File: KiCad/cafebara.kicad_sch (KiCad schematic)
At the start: 26 parts, among them J1 Micro_SD_Card_Det2, J2 USB_C_Receptacle_USB2.0_14P, J3 PROG, J4 505278-1933, J5 I2C, Q1 NMOS, SW1 SW_Push, U3 ATtiny1616-M

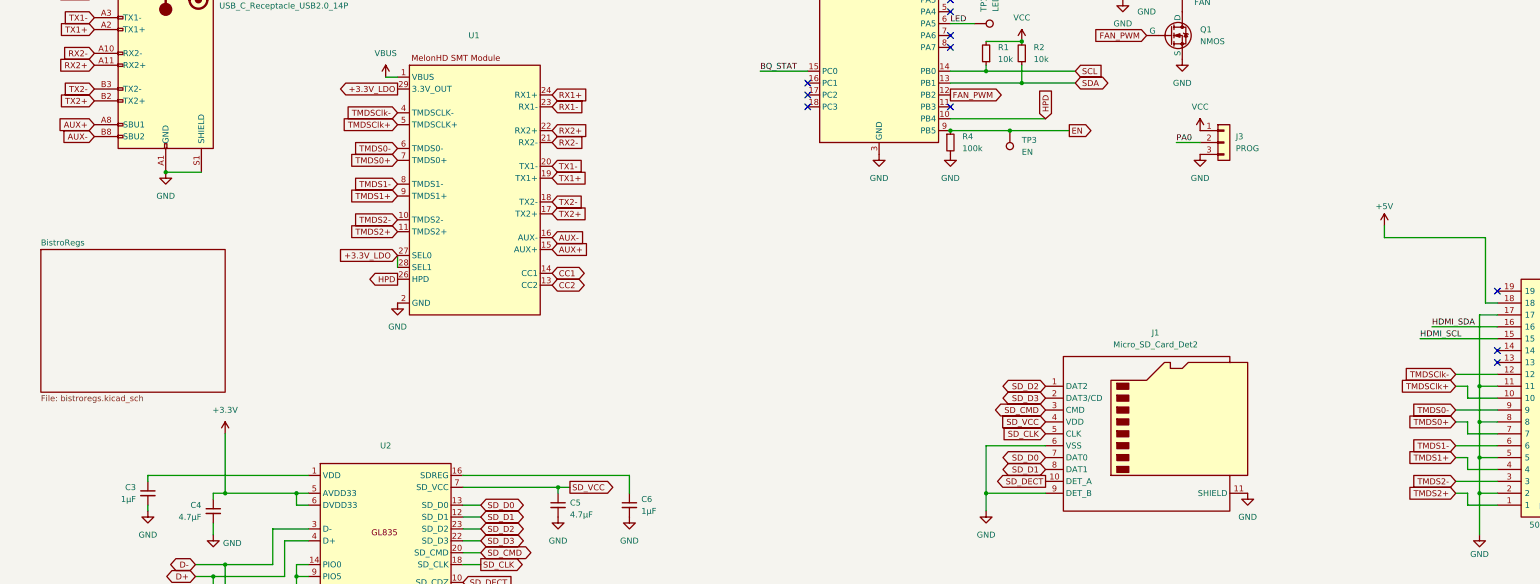
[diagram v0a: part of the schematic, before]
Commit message: Split regs into separate KiCad project
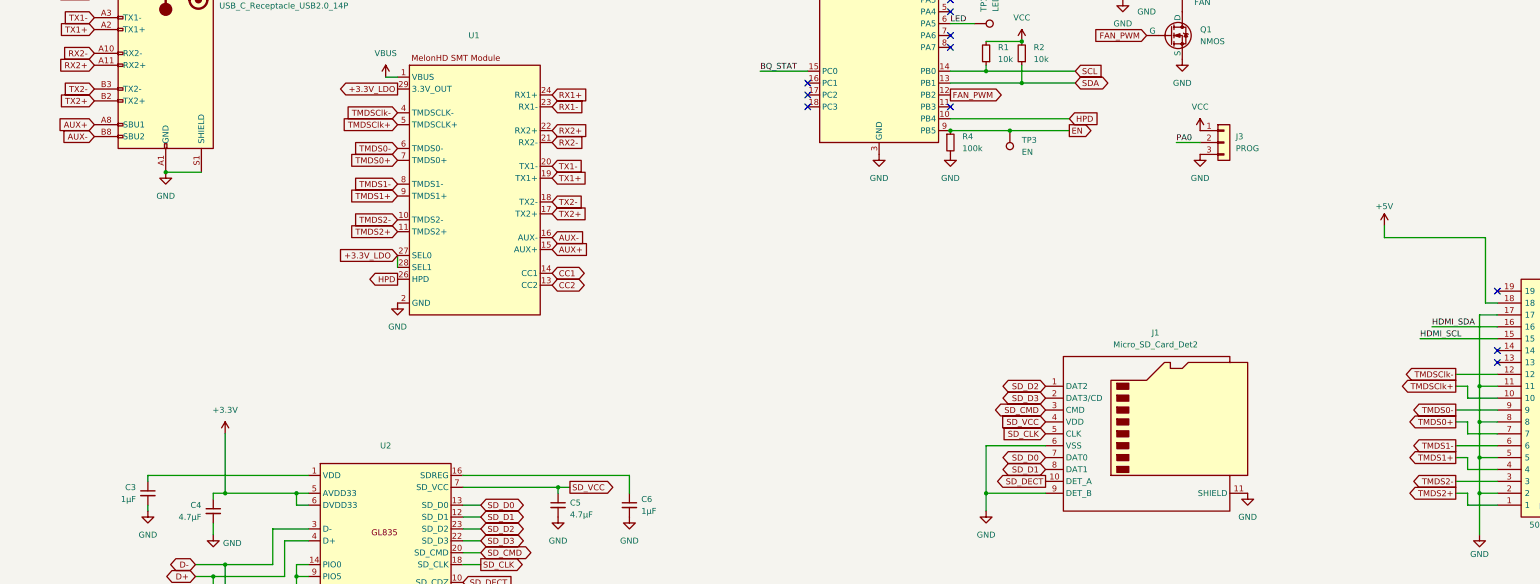
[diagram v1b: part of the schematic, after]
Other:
- removed sheet BistroRegs
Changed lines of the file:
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@@
 	(wire
 		(pts
-			(xy 217.17 76.2) (xy 237.49 76.2)
+			(xy 217.17 76.2) (xy 242.57 76.2)
 		)
 		(stroke
@@
 	)
 	(global_label "TMDS1-"
-		(shape input)
+		(shape output)
 		(at 325.12 146.05 180)
 		(fields_autoplaced yes)
@@
 	)
 	(global_label "TMDS0-"
-		(shape input)
+		(shape output)
 		(at 325.12 138.43 180)
 		(fields_autoplaced yes)
@@
 	)
 	(global_label "TMDS1+"
-		(shape input)
+		(shape output)
 		(at 325.12 148.59 180)
 		(fields_autoplaced yes)
@@
 	(global_label "HPD"
 		(shape input)
-		(at 237.49 76.2 90)
+		(at 242.57 76.2 0)
 		(fields_autoplaced yes)
 		(effects
@@
 		)
 		(property "Intersheetrefs" "${INTERSHEET_REFS}"
-			(at 237.49 69.3443 90)
+			(at 249.4257 76.2 0)
 			(effects
 				(font
@@
 	)
 	(global_label "TMDS2-"
-		(shape input)
+		(shape output)
 		(at 325.12 153.67 180)
 		(fields_autoplaced yes)
@@
 	)
 	(global_label "TMDSClk+"
-		(shape input)
+		(shape output)
 		(at 325.12 133.35 180)
 		(fields_autoplaced yes)
@@
 	)
 	(global_label "TMDSClk-"
-		(shape input)
+		(shape output)
 		(at 325.12 130.81 180)
 		(fields_autoplaced yes)
@@
 	)
 	(global_label "TMDS0+"
-		(shape input)
+		(shape output)
 		(at 325.12 140.97 180)
 		(fields_autoplaced yes)
@@
 	)
 	(global_label "TMDS2+"
-		(shape input)
+		(shape output)
 		(at 325.12 156.21 180)
 		(fields_autoplaced yes)
@@
 				)
 			)
-		)
-	)
-	(sheet
-		(at 22.86 104.14)
-		(size 39.37 30.48)
-		(exclude_from_sim no)
-		(in_bom yes)
-		(on_board yes)
-		(dnp no)
-		(fields_autoplaced yes)
-		(stroke
-			(width 0.1524)
-			(type solid)
-		)
-		(fill
-			(color 0 0 0 0.0000)
-		)
-		(property "Sheetname" "BistroRegs"
-			(at 22.86 103.4284 0)
-			(effects
-				(font
-					(size 1.27 1.27)
-				)
-				(justify left bottom)
-			)
-		)
-		(property "Sheetfile" "bistroregs.kicad_sch"
-			(at 22.86 135.2046 0)
-			(effects
-				(font
-					(size 1.27 1.27)
-				)
-				(justify left top)
-			)
-		)
-		(instances
-			(project "cafebara"
-				(path "/dcc89f95-4ae4-4756-aa81-33bf4d3c86ca"
-					(page "2")
-				)
-			)

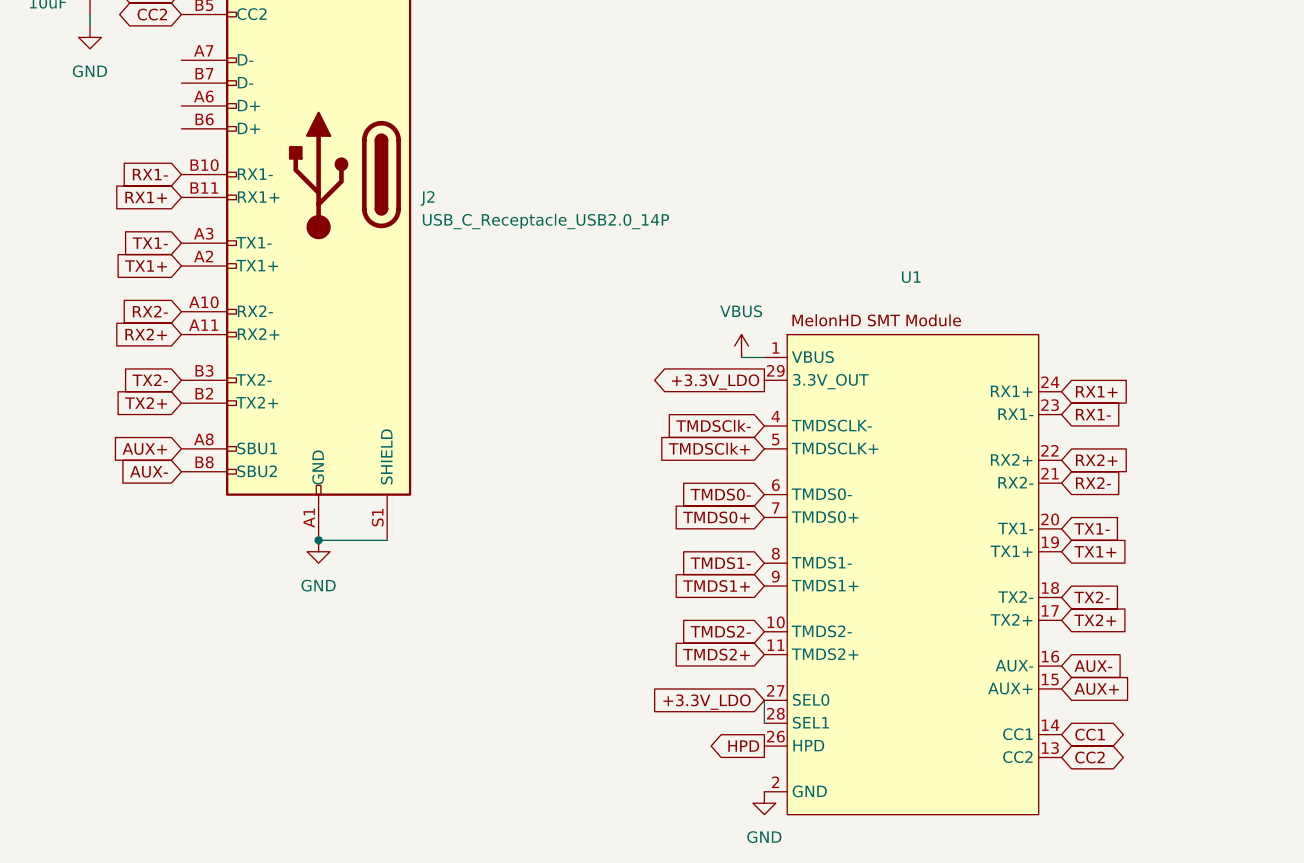
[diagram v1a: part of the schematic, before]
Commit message: Condense main cafebara board
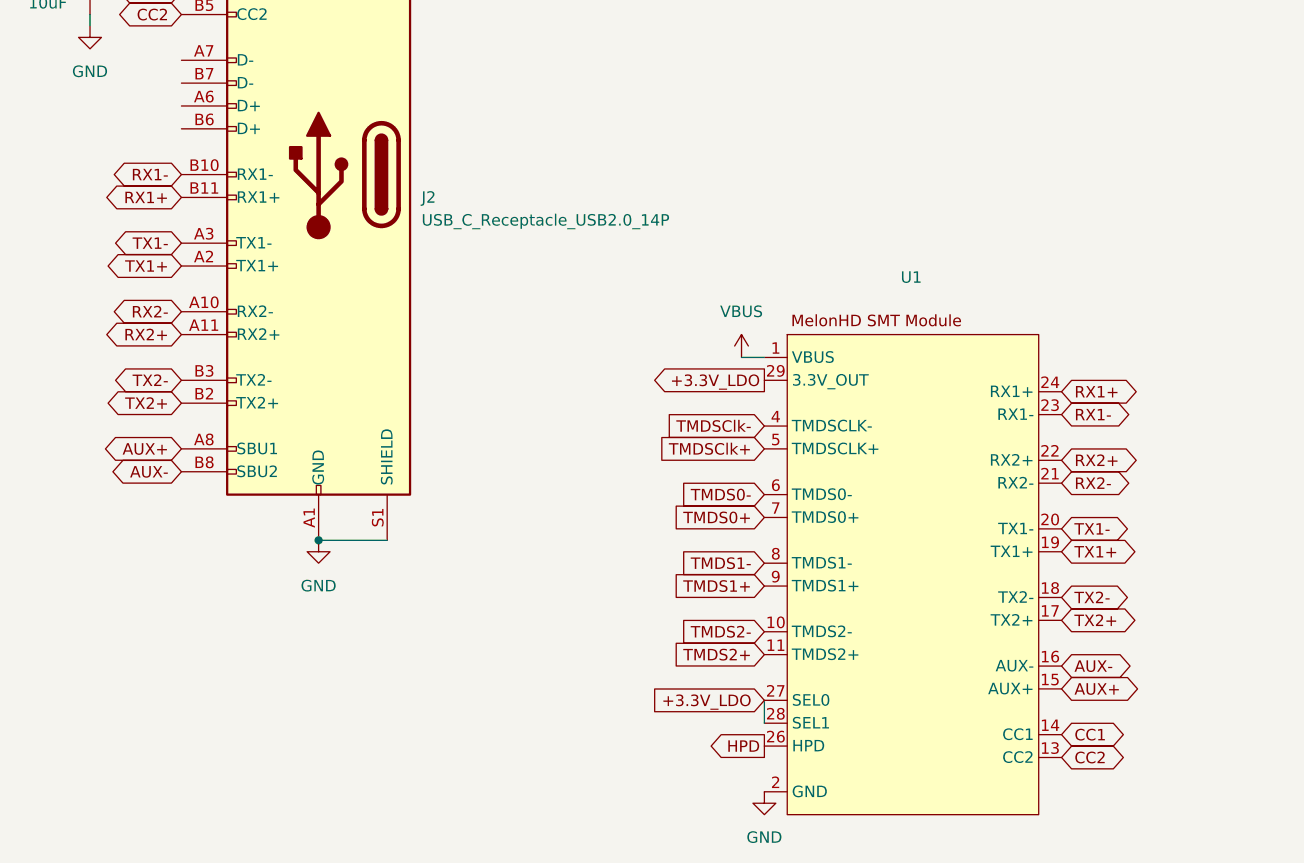
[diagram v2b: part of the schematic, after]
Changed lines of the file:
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@@
 	)
 	(global_label "RX1+"
-		(shape input)
+		(shape bidirectional)
 		(at 34.29 49.53 180)
 		(fields_autoplaced yes)
@@
 	)
 	(global_label "TX2-"
-		(shape input)
+		(shape bidirectional)
 		(at 132.08 93.98 0)
 		(fields_autoplaced yes)
@@
 	)
 	(global_label "TX2-"
-		(shape input)
+		(shape bidirectional)
 		(at 34.29 69.85 180)
 		(fields_autoplaced yes)
@@
 	)
 	(global_label "AUX-"
-		(shape input)
+		(shape bidirectional)
 		(at 34.29 80.01 180)
 		(fields_autoplaced yes)
@@
 	)
 	(global_label "TX1+"
-		(shape input)
+		(shape bidirectional)
 		(at 132.08 88.9 0)
 		(fields_autoplaced yes)
@@
 	)
 	(global_label "RX1-"
-		(shape input)
+		(shape bidirectional)
 		(at 34.29 46.99 180)
 		(fields_autoplaced yes)
@@
 	)
 	(global_label "RX2-"
-		(shape input)
+		(shape bidirectional)
 		(at 132.08 81.28 0)
 		(fields_autoplaced yes)
@@
 	)
 	(global_label "TX1-"
-		(shape input)
+		(shape bidirectional)
 		(at 34.29 54.61 180)
 		(fields_autoplaced yes)
@@
 	)
 	(global_label "TX2+"
-		(shape input)
+		(shape bidirectional)
 		(at 34.29 72.39 180)
 		(fields_autoplaced yes)
@@
 	)
 	(global_label "RX1-"
-		(shape input)
+		(shape bidirectional)
 		(at 132.08 73.66 0)
 		(fields_autoplaced yes)
@@
 	)
 	(global_label "AUX+"
-		(shape input)
+		(shape bidirectional)
 		(at 132.08 104.14 0)
 		(fields_autoplaced yes)
@@
 	)
 	(global_label "AUX-"
-		(shape input)
+		(shape bidirectional)
 		(at 132.08 101.6 0)
 		(fields_autoplaced yes)
@@
 	)
 	(global_label "RX2+"
-		(shape input)
+		(shape bidirectional)
 		(at 34.29 64.77 180)
 		(fields_autoplaced yes)
@@
 	)
 	(global_label "AUX+"
-		(shape input)
+		(shape bidirectional)
 		(at 34.29 77.47 180)
 		(fields_autoplaced yes)
@@
 	)
 	(global_label "RX2+"
-		(shape input)
+		(shape bidirectional)
 		(at 132.08 78.74 0)
 		(fields_autoplaced yes)
@@
 	)
 	(global_label "TX2+"
-		(shape input)
+		(shape bidirectional)
 		(at 132.08 96.52 0)
 		(fields_autoplaced yes)
@@
 	)
 	(global_label "RX1+"
-		(shape input)
+		(shape bidirectional)
 		(at 132.08 71.12 0)
 		(fields_autoplaced yes)
@@
 	)
 	(global_label "TX1+"
-		(shape input)
+		(shape bidirectional)
 		(at 34.29 57.15 180)
 		(fields_autoplaced yes)
@@
 	)
 	(global_label "TX1-"
-		(shape input)
+		(shape bidirectional)
 		(at 132.08 86.36 0)
 		(fields_autoplaced yes)
@@
 	)
 	(global_label "RX2-"
-		(shape input)
+		(shape bidirectional)
 		(at 34.29 62.23 180)
 		(fields_autoplaced yes)

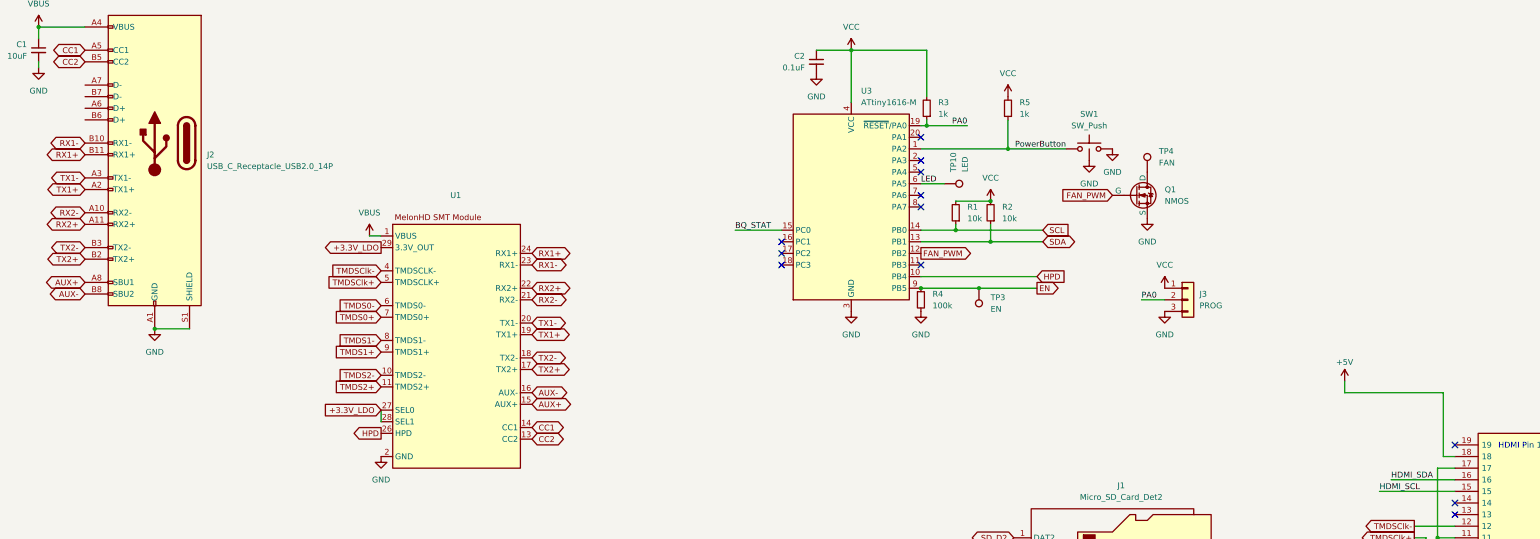
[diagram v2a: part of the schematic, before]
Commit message: Finish HDMI mux, misc improvements to cafebara
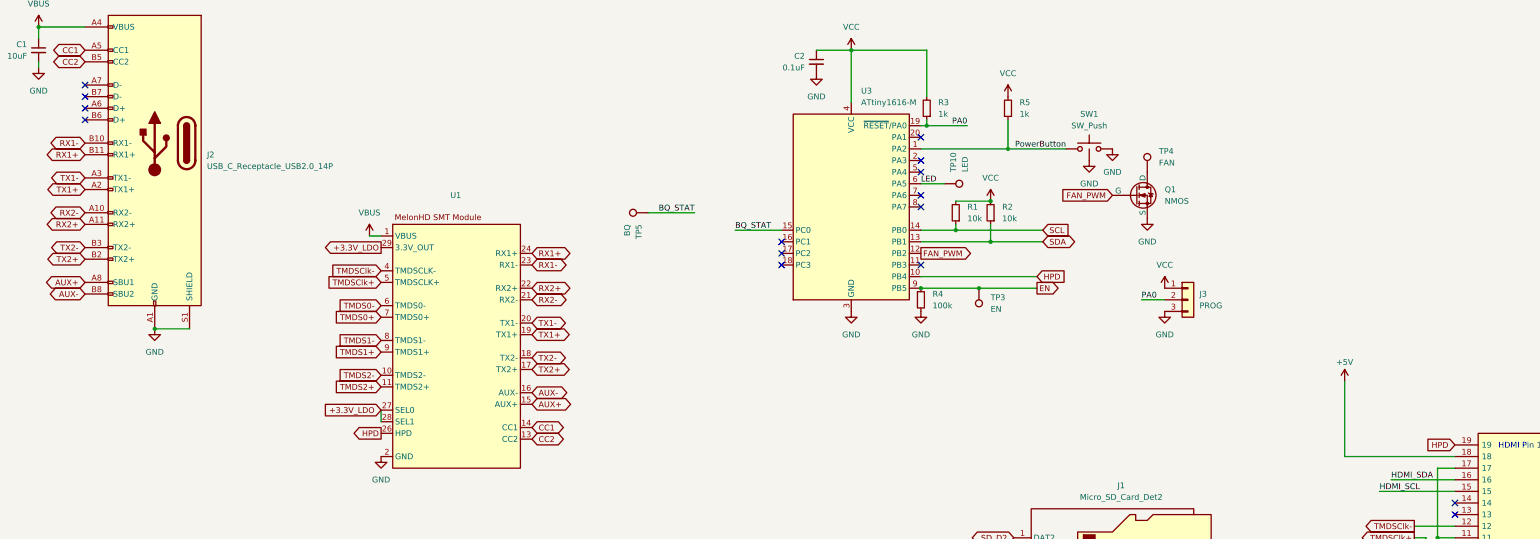
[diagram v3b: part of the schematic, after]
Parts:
- added TP5: BQ, cafebara:TestPoint_Pad_D1.0mm_Small, symbol Connector:TestPoint
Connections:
- net BQ_STAT: now also TP5.1
- net HPD: now also J4.19
- no-connect marks 12 -> 15
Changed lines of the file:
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@@
 	)
 	(no_connect
+		(at 34.29 41.91)
+	)
+	(no_connect
 		(at 217.17 73.66)
 	)
@@
 	)
 	(no_connect
+		(at 34.29 39.37)
+	)
+	(no_connect
+		(at 34.29 36.83)
+	)
+	(no_connect
 		(at 217.17 58.42)
 	)
 	(no_connect
-		(at 334.01 113.03)
+		(at 34.29 34.29)
 	)
 	(no_connect
@@
 	(wire
 		(pts
+			(xy 157.48 62.23) (xy 167.64 62.23)
+		)
+		(stroke
+			(width 0)
+			(type default)
+		)
+	)
+	(wire
+		(pts
 			(xy 62.23 171.45) (xy 62.23 176.53)
 		)
@@
 	(wire
 		(pts
-			(xy 309.88 101.6) (xy 331.47 101.6)
-		)
-		(stroke
-			(width 0)
-			(type default)
-		)
-	)
-	(wire
-		(pts
 			(xy 327.66 148.59) (xy 327.66 151.13)
 		)
@@
 	(wire
 		(pts
-			(xy 331.47 115.57) (xy 334.01 115.57)
+			(xy 309.88 115.57) (xy 334.01 115.57)
 		)
 		(stroke
@@
 	(wire
 		(pts
-			(xy 331.47 115.57) (xy 331.47 101.6)
-		)
-		(stroke
-			(width 0)
-			(type default)
-		)
-	)
-	(wire
-		(pts
-			(xy 309.88 99.06) (xy 309.88 101.6)
+			(xy 309.88 99.06) (xy 309.88 115.57)
 		)
 		(stroke
@@
 	)
 	(label "BQ_STAT"
+		(at 167.64 62.23 180)
+		(effects
+			(font
+				(size 1.27 1.27)
+			)
+			(justify right bottom)
+		)
+	)
+	(label "BQ_STAT"
 		(at 176.53 66.04 0)
 		(effects
@@
 		)
 	)
+	(global_label "HPD"
+		(shape input)
+		(at 334.01 113.03 180)
+		(fields_autoplaced yes)
+		(effects
+			(font
+				(size 1.27 1.27)
+			)
+			(justify right)
+		)
+		(property "Intersheetrefs" "${INTERSHEET_REFS}"
+			(at 327.1543 113.03 0)
+			(effects
+				(font
+					(size 1.27 1.27)
+				)
+				(justify right)
+				(hide yes)
+			)
+		)
+	)
 	(global_label "AUX-"
 		(shape bidirectional)
@@
 					(unit 1)
 				)
+			)
+		)
+	)
+	(symbol
+		(lib_id "Connector:TestPoint")
+		(at 157.48 62.23 90)
+		(unit 1)
+		(exclude_from_sim no)
+		(in_bom yes)
+		(on_board yes)
+		(dnp no)
+		(property "Reference" "TP5"
+			(at 155.4481 64.77 0)
+			(effects
+				(font
+					(size 1.27 1.27)
+				)
+				(justify right)
+			)
+		)
+		(property "Value" "BQ"
+			(at 152.9081 64.77 0)
+			(effects
+				(font
+					(size 1.27 1.27)
+				)
+				(justify right)
+			)
+		)
+		(property "Footprint" "cafebara:TestPoint_Pad_D1.0mm_Small"
+			(at 157.48 57.15 0)
+			(effects
+				(font
+					(size 1.27 1.27)
+				)
+				(hide yes)
+			)
+		)
+		(property "Datasheet" "~"
+			(at 157.48 57.15 0)
+			(effects
+				(font
+					(size 1.27 1.27)
+				)
+				(hide yes)
+			)
+		)
+		(property "Description" "test point"
+			(at 157.48 62.23 0)
+			(effects
+				(font
+					(size 1.27 1.27)
+				)
+				(hide yes)
+			)
+		)
+		(pin "1"
+		)
+		(instances
+			(project "cafebara"
+				(path "/dcc89f95-4ae4-4756-aa81-33bf4d3c86ca"
+					(reference "TP5")
+					(unit 1)
+				)
